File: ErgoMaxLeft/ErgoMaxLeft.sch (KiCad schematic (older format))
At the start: 102 parts, among them J1 PJ-320A, K1 KEYSW, K10 KEYSW, K11 KEYSW, K12 KEYSW, K13 KEYSW, K14 KEYSW, K15 KEYSW, K16 KEYSW, K17 KEYSW, K18 KEYSW, K19 KEYSW, K2 KEYSW, K20 KEYSW, K21 KEYSW, K22 KEYSW, K23 KEYSW, K24 KEYSW, K25 KEYSW, K26 KEYSW, K27 KEYSW, K28 KEYSW, K29 KEYSW, K3 KEYSW, K30 KEYSW, K31 KEYSW, K32 KEYSW, K33 KEYSW, K34 KEYSW, K35 KEYSW, K36 KEYSW, K37 KEYSW, K38 KEYSW, K39 KEYSW, K4 KEYSW, K40 KEYSW, K41 KEYSW, K42 KEYSW, K43 KEYSW, K44 KEYSW, K5 KEYSW, K6 KEYSW, K7 KEYSW, K8 KEYSW, K9 KEYSW, U1 ProMicro

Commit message: add add values for main keys on PCB
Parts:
- K1, K6: value KEYSW -> F1
- K10: value KEYSW -> 3 #
- K11: value KEYSW -> 4 $
- K12: value KEYSW -> 5 %
- K15: value KEYSW -> Q
- K16: value KEYSW -> W
- K17: value KEYSW -> E
- K18: value KEYSW -> R
- K19: value KEYSW -> T
- K2: value KEYSW -> F2
- K22: value KEYSW -> A
- K23: value KEYSW -> S
- K24: value KEYSW -> D
- K25: value KEYSW -> F
- K26: value KEYSW -> G
- K3: value KEYSW -> F3
- K30: value KEYSW -> Z
- K31: value KEYSW -> X
- K32: value KEYSW -> C
- K33: value KEYSW -> V
- K34: value KEYSW -> B
- K4: value KEYSW -> F4
- K5: value KEYSW -> F5
- K8: value KEYSW -> 1 !
- K9: value KEYSW -> 2 @
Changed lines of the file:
@@
 EESchema Schematic File Version 4
+LIBS:ErgoMaxLeft-cache
 EELAYER 26 0
 EELAYER END
@@
 P 6050 1700
 F 0 "K1" H 6050 1933 60  0000 C CNN
-F 1 "KEYSW" H 6050 1600 60  0001 C CNN
+F 1 "F1" H 6050 1600 60  0001 C CNN
 F 2 "ErgoMax:Kailh_MX_Socket" H 6050 1700 60  0001 C CNN
 F 3 "" H 6050 1700 60  0000 C CNN
@@
 P 5200 1700
 F 0 "K2" H 5200 1933 60  0000 C CNN
-F 1 "KEYSW" H 5200 1600 60  0001 C CNN
+F 1 "F2" H 5200 1600 60  0001 C CNN
 F 2 "ErgoMax:Kailh_MX_Socket" H 5200 1700 60  0001 C CNN
 F 3 "" H 5200 1700 60  0000 C CNN
@@
 P 4350 1700
 F 0 "K3" H 4350 1933 60  0000 C CNN
-F 1 "KEYSW" H 4350 1600 60  0001 C CNN
+F 1 "F3" H 4350 1600 60  0001 C CNN
 F 2 "ErgoMax:Kailh_MX_Socket" H 4350 1700 60  0001 C CNN
 F 3 "" H 4350 1700 60  0000 C CNN
@@
 P 3500 1700
 F 0 "K4" H 3500 1933 60  0000 C CNN
-F 1 "KEYSW" H 3500 1600 60  0001 C CNN
+F 1 "F4" H 3500 1600 60  0001 C CNN
 F 2 "ErgoMax:Kailh_MX_Socket" H 3500 1700 60  0001 C CNN
 F 3 "" H 3500 1700 60  0000 C CNN
@@
 P 2650 1700
 F 0 "K5" H 2650 1933 60  0000 C CNN
-F 1 "KEYSW" H 2650 1600 60  0001 C CNN
+F 1 "F5" H 2650 1600 60  0001 C CNN
 F 2 "ErgoMax:Kailh_MX_Socket" H 2650 1700 60  0001 C CNN
 F 3 "" H 2650 1700 60  0000 C CNN
@@
 P 1800 1700
 F 0 "K6" H 1800 1933 60  0000 C CNN
-F 1 "KEYSW" H 1800 1600 60  0001 C CNN
+F 1 "F1" H 1800 1600 60  0001 C CNN
 F 2 "ErgoMax:Kailh_MX_Socket" H 1800 1700 60  0001 C CNN
 F 3 "" H 1800 1700 60  0000 C CNN
@@
 P 6050 2300
 F 0 "K8" H 6050 2500 60  0000 C CNN
-F 1 "KEYSW" H 6050 2200 60  0001 C CNN
+F 1 "1 !" H 6050 2200 60  0001 C CNN
 F 2 "ErgoMax:Kailh_MX_Socket" H 6050 2300 60  0001 C CNN
 F 3 "" H 6050 2300 60  0000 C CNN
@@
 P 5200 2300
 F 0 "K9" H 5200 2500 60  0000 C CNN
-F 1 "KEYSW" H 5200 2200 60  0001 C CNN
+F 1 "2 @" H 5200 2200 60  0001 C CNN
 F 2 "ErgoMax:Kailh_MX_Socket" H 5200 2300 60  0001 C CNN
 F 3 "" H 5200 2300 60  0000 C CNN
@@
 P 4350 2300
 F 0 "K10" H 4350 2500 60  0000 C CNN
-F 1 "KEYSW" H 4350 2200 60  0001 C CNN
+F 1 "3 #" H 4350 2200 60  0001 C CNN
 F 2 "ErgoMax:Kailh_MX_Socket" H 4350 2300 60  0001 C CNN
 F 3 "" H 4350 2300 60  0000 C CNN
@@
 P 3500 2300
 F 0 "K11" H 3500 2500 60  0000 C CNN
-F 1 "KEYSW" H 3500 2200 60  0001 C CNN
+F 1 "4 $" H 3500 2200 60  0001 C CNN
 F 2 "ErgoMax:Kailh_MX_Socket" H 3500 2300 60  0001 C CNN
 F 3 "" H 3500 2300 60  0000 C CNN
@@
 P 2650 2300
 F 0 "K12" H 2650 2500 60  0000 C CNN
-F 1 "KEYSW" H 2650 2200 60  0001 C CNN
+F 1 "5 %" H 2650 2200 60  0001 C CNN
 F 2 "ErgoMax:Kailh_MX_Socket" H 2650 2300 60  0001 C CNN
 F 3 "" H 2650 2300 60  0000 C CNN
@@
 P 6050 2900
 F 0 "K15" H 6050 3100 60  0000 C CNN
-F 1 "KEYSW" H 6050 2800 60  0001 C CNN
+F 1 "Q" H 6050 2800 60  0001 C CNN
 F 2 "ErgoMax:Kailh_MX_Socket" H 6050 2900 60  0001 C CNN
 F 3 "" H 6050 2900 60  0000 C CNN
@@
 P 5200 2900
 F 0 "K16" H 5200 3100 60  0000 C CNN
-F 1 "KEYSW" H 5200 2800 60  0001 C CNN
+F 1 "W" H 5200 2800 60  0001 C CNN
 F 2 "ErgoMax:Kailh_MX_Socket" H 5200 2900 60  0001 C CNN
 F 3 "" H 5200 2900 60  0000 C CNN
@@
 P 4350 2900
 F 0 "K17" H 4350 3100 60  0000 C CNN
-F 1 "KEYSW" H 4350 2800 60  0001 C CNN
+F 1 "E" H 4350 2800 60  0001 C CNN
 F 2 "ErgoMax:Kailh_MX_Socket" H 4350 2900 60  0001 C CNN
 F 3 "" H 4350 2900 60  0000 C CNN
@@
 P 3500 2900
 F 0 "K18" H 3500 3100 60  0000 C CNN
-F 1 "KEYSW" H 3500 2800 60  0001 C CNN
+F 1 "R" H 3500 2800 60  0001 C CNN
 F 2 "ErgoMax:Kailh_MX_Socket" H 3500 2900 60  0001 C CNN
 F 3 "" H 3500 2900 60  0000 C CNN
@@
 P 2650 2900
 F 0 "K19" H 2650 3100 60  0000 C CNN
-F 1 "KEYSW" H 2650 2800 60  0001 C CNN
+F 1 "T" H 2650 2800 60  0001 C CNN
 F 2 "ErgoMax:Kailh_MX_Socket" H 2650 2900 60  0001 C CNN
 F 3 "" H 2650 2900 60  0000 C CNN
@@
 P 6050 3500
 F 0 "K22" H 6050 3700 60  0000 C CNN
-F 1 "KEYSW" H 6050 3400 60  0001 C CNN
+F 1 "A" H 6050 3400 60  0001 C CNN
 F 2 "ErgoMax:Kailh_MX_Socket" H 6050 3500 60  0001 C CNN
 F 3 "" H 6050 3500 60  0000 C CNN
@@
 P 5200 3500
 F 0 "K23" H 5200 3700 60  0000 C CNN
-F 1 "KEYSW" H 5200 3400 60  0001 C CNN
+F 1 "S" H 5200 3400 60  0001 C CNN
 F 2 "ErgoMax:Kailh_MX_Socket" H 5200 3500 60  0001 C CNN
 F 3 "" H 5200 3500 60  0000 C CNN
@@
 P 4350 3500
 F 0 "K24" H 4350 3700 60  0000 C CNN
-F 1 "KEYSW" H 4350 3400 60  0001 C CNN
+F 1 "D" H 4350 3400 60  0001 C CNN
 F 2 "ErgoMax:Kailh_MX_Socket" H 4350 3500 60  0001 C CNN
 F 3 "" H 4350 3500 60  0000 C CNN
@@
 P 3500 3500
 F 0 "K25" H 3500 3700 60  0000 C CNN
-F 1 "KEYSW" H 3500 3400 60  0001 C CNN
+F 1 "F" H 3500 3400 60  0001 C CNN
 F 2 "ErgoMax:Kailh_MX_Socket" H 3500 3500 60  0001 C CNN
 F 3 "" H 3500 3500 60  0000 C CNN
@@
 P 2650 3500
 F 0 "K26" H 2650 3700 60  0000 C CNN
-F 1 "KEYSW" H 2650 3400 60  0001 C CNN
+F 1 "G" H 2650 3400 60  0001 C CNN
 F 2 "ErgoMax:Kailh_MX_Socket" H 2650 3500 60  0001 C CNN
 F 3 "" H 2650 3500 60  0000 C CNN
@@
 P 6050 4100
 F 0 "K30" H 6050 4300 60  0000 C CNN
-F 1 "KEYSW" H 6050 4000 60  0001 C CNN
+F 1 "Z" H 6050 4000 60  0001 C CNN
 F 2 "ErgoMax:Kailh_MX_Socket" H 6050 4100 60  0001 C CNN
 F 3 "" H 6050 4100 60  0000 C CNN
@@
 P 5200 4100
 F 0 "K31" H 5200 4300 60  0000 C CNN
-F 1 "KEYSW" H 5200 4000 60  0001 C CNN
+F 1 "X" H 5200 4000 60  0001 C CNN
 F 2 "ErgoMax:Kailh_MX_Socket" H 5200 4100 60  0001 C CNN
 F 3 "" H 5200 4100 60  0000 C CNN
@@
 P 4350 4100
 F 0 "K32" H 4350 4300 60  0000 C CNN
-F 1 "KEYSW" H 4350 4000 60  0001 C CNN
+F 1 "C" H 4350 4000 60  0001 C CNN
 F 2 "ErgoMax:Kailh_MX_Socket" H 4350 4100 60  0001 C CNN
 F 3 "" H 4350 4100 60  0000 C CNN
@@
 P 3500 4100
 F 0 "K33" H 3500 4300 60  0000 C CNN
-F 1 "KEYSW" H 3500 4000 60  0001 C CNN
+F 1 "V" H 3500 4000 60  0001 C CNN
 F 2 "ErgoMax:Kailh_MX_Socket" H 3500 4100 60  0001 C CNN
 F 3 "" H 3500 4100 60  0000 C CNN
@@
 P 2650 4100
 F 0 "K34" H 2650 4300 60  0000 C CNN
-F 1 "KEYSW" H 2650 4000 60  0001 C CNN
+F 1 "B" H 2650 4000 60  0001 C CNN
 F 2 "ErgoMax:Kailh_MX_Socket" H 2650 4100 60  0001 C CNN
 F 3 "" H 2650 4100 60  0000 C CNN

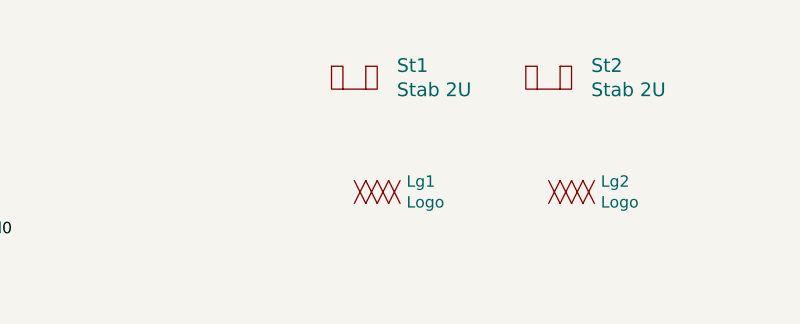
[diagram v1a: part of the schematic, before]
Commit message: move logos to front side of left and right PCB, add left/right writings
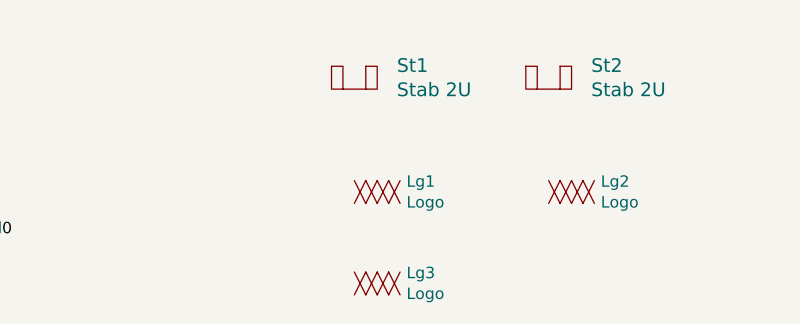
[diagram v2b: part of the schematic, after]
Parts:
- added Lg3: Logo, ErgoMax:LeftSideText, symbol ErgoMax:Logo
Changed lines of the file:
@@
 Wire Wire Line
 	6600 4400 7900 4400
+$Comp
+L ErgoMax:Logo Lg3
+U 1 1 5C036DC6
+P 9100 5650
+F 0 "Lg3" H 9228 5696 50  0000 L CNN
+F 1 "Logo" H 9228 5605 50  0000 L CNN
+F 2 "ErgoMax:LeftSideText" H 9100 5550 50  0001 C CNN
+F 3 "" H 9100 5550 50  0001 C CNN
+	1    9100 5650
+	1    0    0    -1
+$EndComp
 $EndSCHEMATC
